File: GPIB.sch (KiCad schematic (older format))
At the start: 24 parts, among them P1 CONN_6, P2 CONN_2, P3 CONN_4X2, P4 CONN_CENTRONICS_24, SW1 SW_RESET, SW2 SW_BOOTL, U5 STM32F072CBT6, U6 SN75160B, U7 SN75162B

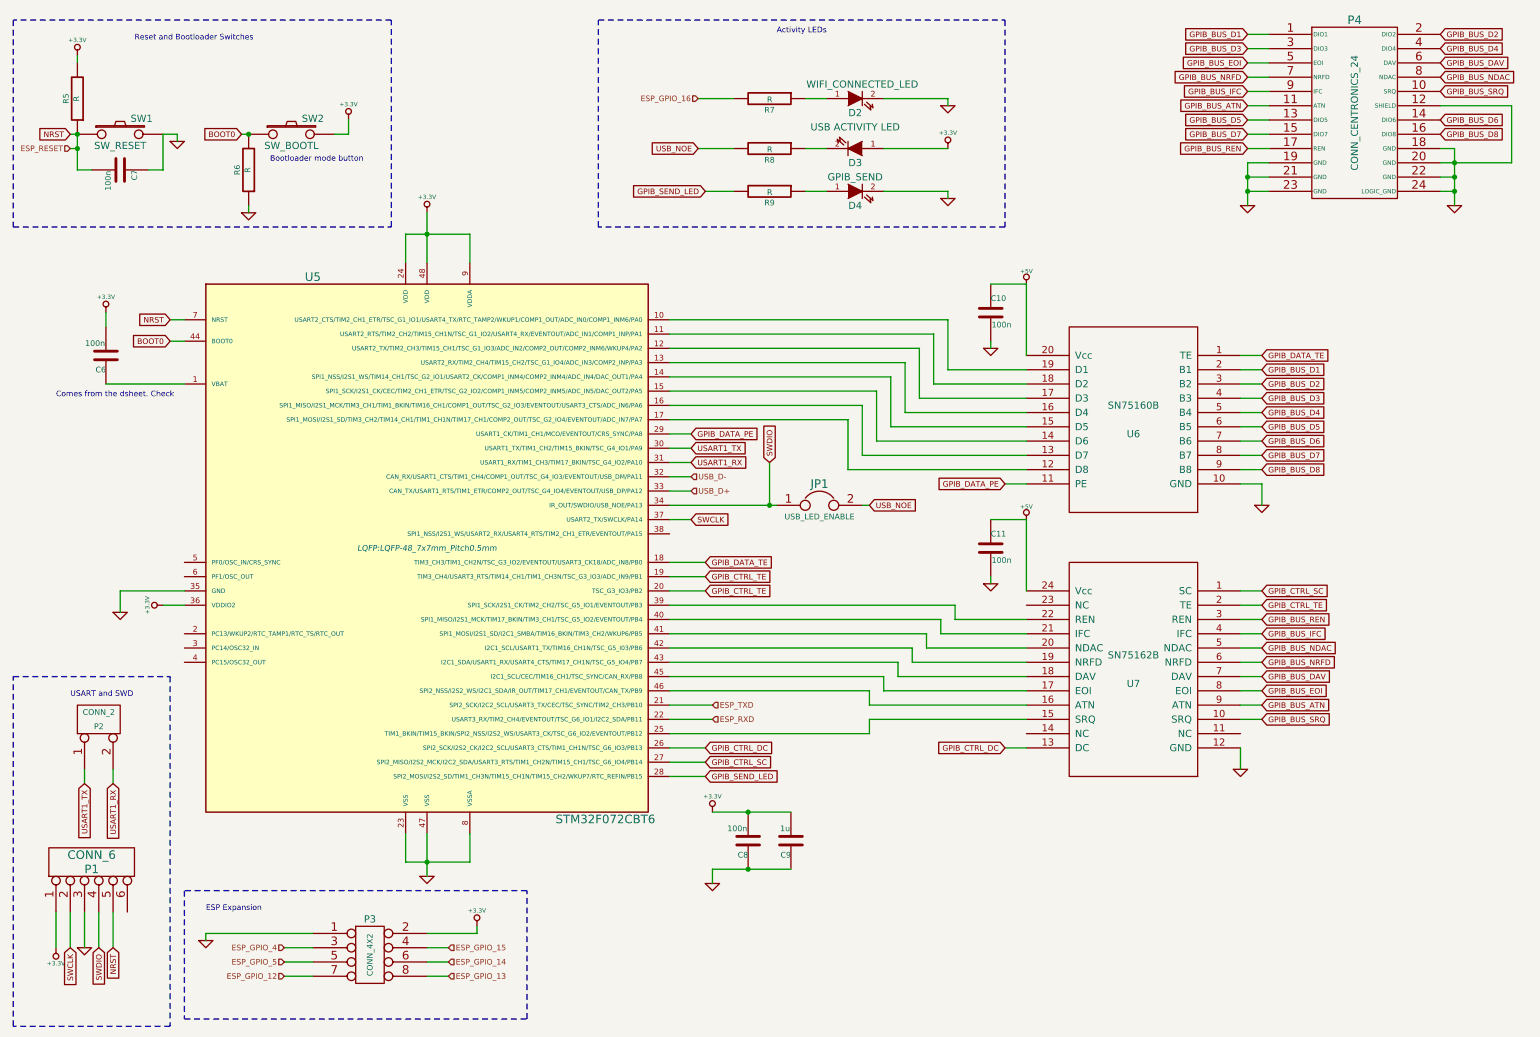
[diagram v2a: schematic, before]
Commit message: Remove Barrel Jack and associated power circuits. Unnecessary for now and add a lot of complexity / BOM cost
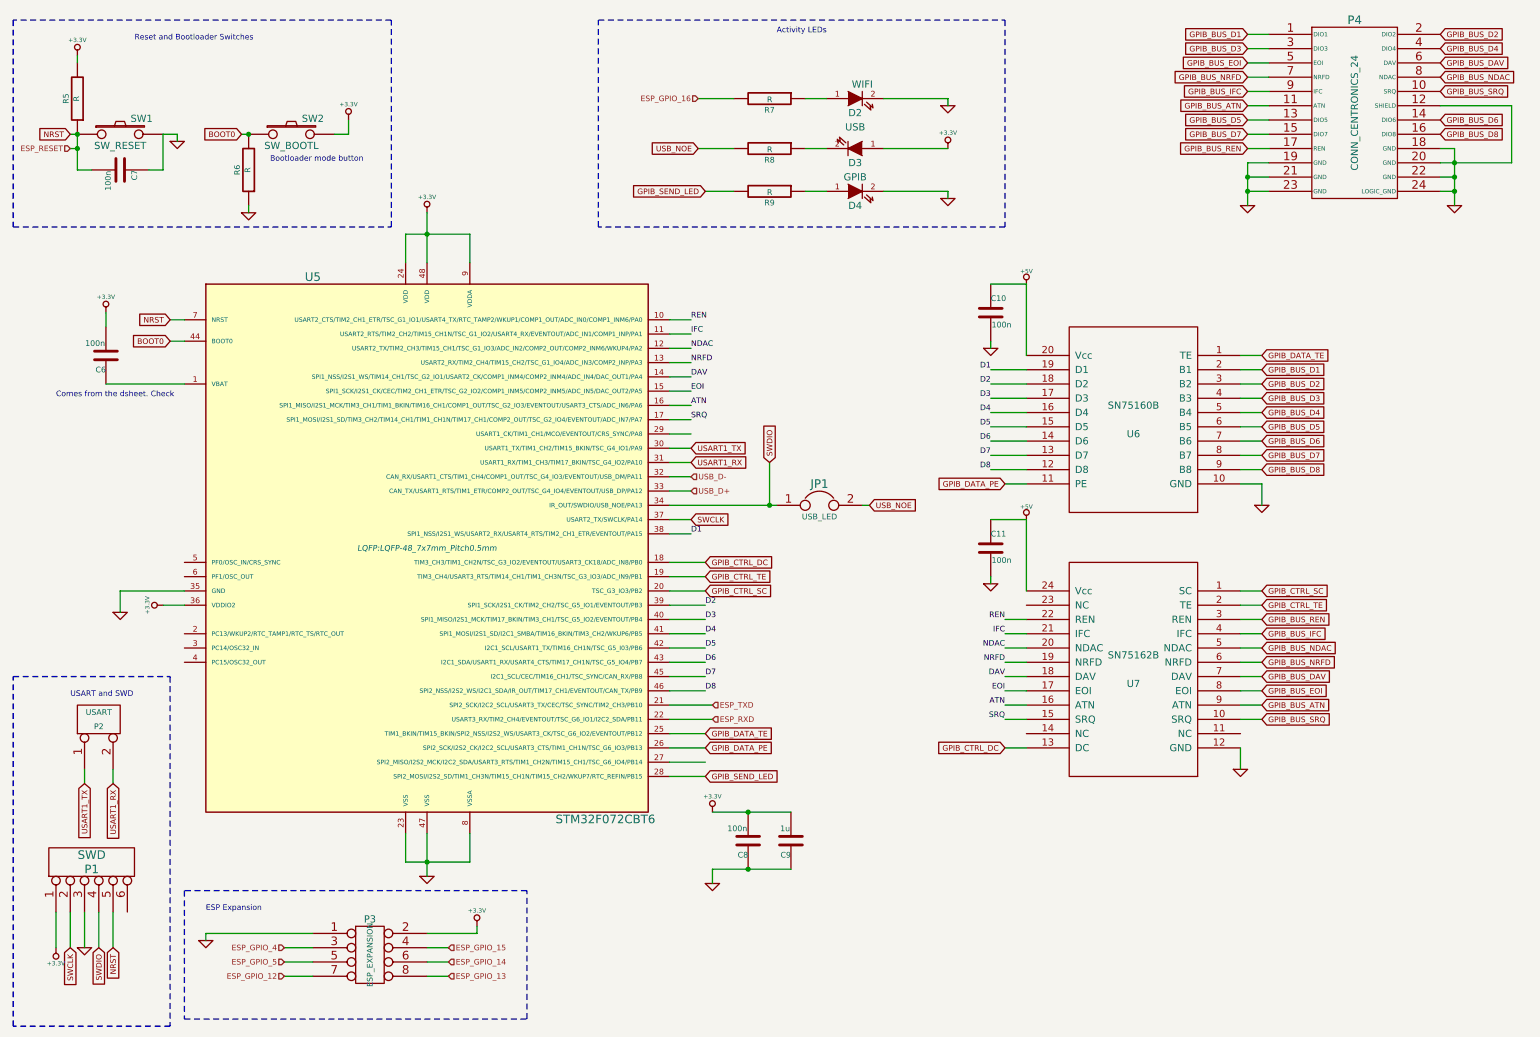
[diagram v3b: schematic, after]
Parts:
- D2: value WIFI_CONNECTED_LED -> WIFI
- D3: value USB ACTIVITY LED -> USB
- D4: value GPIB_SEND -> GPIB
- JP1: value USB_LED_ENABLE -> USB_LED
- P1: value CONN_6 -> SWD
- P2: value CONN_2 -> USART
- P3: value CONN_4X2 -> ESP_EXPANSION
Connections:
- net GPIB_CTRL_DC: now also U5.18 (TIM3_CH3/TIM1_CH2N/TSC_G3_IO2/EVENTOUT/USART3_CK18/ADC_IN8/PB0); no longer U5.26 (SPI2_SCK/I2S2_CK/I2C2_SCL/USART3_CTS/TIM1_CH1N/TSC_G6_IO3/PB13)
- net GPIB_CTRL_SC: now also U5.20 (TSC_G3_IO3/PB2); no longer U5.27 (SPI2_MISO/I2S2_MCK/I2C2_SDA/USART3_RTS/TIM1_CH2N/TIM15_CH1/TSC_G6_IO4/PB14)
- net GPIB_CTRL_TE: no longer U5.20 (TSC_G3_IO3/PB2)
- net GPIB_DATA_PE: now also U5.26 (SPI2_SCK/I2S2_CK/I2C2_SCL/USART3_CTS/TIM1_CH1N/TSC_G6_IO3/PB13); no longer U5.29 (USART1_CK/TIM1_CH1/MCO/EVENTOUT/CRS_SYNC/PA8)
- net GPIB_DATA_TE: now also U5.25 (TIM1_BKIN/TIM15_BKIN/SPI2_NSS/I2S2_WS/USART3_CK/TSC_G6_IO2/EVENTOUT/PB12); no longer U5.18 (TIM3_CH3/TIM1_CH2N/TSC_G3_IO2/EVENTOUT/USART3_CK18/ADC_IN8/PB0)
- net D8: now reaches U6.12 (D8)
- net D8: now also U5.46 (SPI2_NSS/I2S2_WS/I2C1_SDA/IR_OUT/TIM17_CH1/EVENTOUT/CAN_TX/PB9); no longer U5.17 (SPI1_MOSI/I2S1_SD/TIM3_CH2/TIM14_CH1/TIM1_CH1N/TIM17_CH1/COMP2_OUT/TSC_G2_IO4/EVENTOUT/ADC_IN7/PA7)
- net ATN: now reaches U5.16 (SPI1_MISO/I2S1_MCK/TIM3_CH1/TIM1_BKIN/TIM16_CH1/COMP1_OUT/TSC_G2_IO3/EVENTOUT/USART3_CTS/ADC_IN6/PA6)
- net ATN: now also U7.16 (ATN); no longer U6.13 (D7)
- net D6: now reaches U6.14 (D6)
- net D6: now also U5.43 (I2C1_SDA/USART1_RX/USART4_CTS/TIM17_CH1N/TSC_G5_IO4/PB7); no longer U5.15 (SPI1_SCK/I2S1_CK/CEC/TIM2_CH1_ETR/TSC_G2_IO2/COMP1_INM5/COMP2_INM5/ADC_IN5/DAC_OUT2/PA5)
- net D5: now reaches U6.15 (D5)
- net D5: now also U5.42 (I2C1_SCL/USART1_TX/TIM16_CH1N/TSC_G5_I03/PB6); no longer U5.14 (SPI1_NSS/I2S1_WS/TIM14_CH1/TSC_G2_IO1/USART2_CK/COMP1_INM4/COMP2_INM4/ADC_IN4/DAC_OUT1/PA4)
- net D4: now reaches U6.16 (D4)
- net D4: now also U5.41 (SPI1_MOSI/I2S1_SD/I2C1_SMBA/TIM16_BKIN/TIM3_CH2/WKUP6/PB5); no longer U5.13 (USART2_RX/TIM2_CH4/TIM15_CH2/TSC_G1_IO4/ADC_IN3/COMP2_INP/PA3)
- net D3: now reaches U6.17 (D3)
- net D3: now also U5.40 (SPI1_MISO/I2S1_MCK/TIM17_BKIN/TIM3_CH1/TSC_G5_IO2/EVENTOUT/PB4); no longer U5.12 (USART2_TX/TIM2_CH3/TIM15_CH1/TSC_G1_IO3/ADC_IN2/COMP2_OUT/COMP2_INM6/WKUP4/PA2)
- net D2: now reaches U6.18 (D2)
- net D2: now also U5.39 (SPI1_SCK/I2S1_CK/TIM2_CH2/TSC_G5_IO1/EVENTOUT/PB3); no longer U5.11 (USART2_RTS/TIM2_CH2/TIM15_CH1N/TSC_G1_IO2/USART4_RX/EVENTOUT/ADC_IN1/COMP1_INP/PA1)
- net D1: now reaches U6.19 (D1)
- net D1: now also U5.38 (SPI1_NSS/I2S1_WS/USART2_RX/USART4_RTS/TIM2_CH1_ETR/EVENTOUT/PA15); no longer U5.10 (USART2_CTS/TIM2_CH1_ETR/TSC_G1_IO1/USART4_TX/RTC_TAMP2/WKUP1/COMP1_OUT/ADC_IN0/COMP1_INM6/PA0)
- net SRQ: now reaches U7.15 (SRQ)
- net SRQ: now also U5.17 (SPI1_MOSI/I2S1_SD/TIM3_CH2/TIM14_CH1/TIM1_CH1N/TIM17_CH1/COMP2_OUT/TSC_G2_IO4/EVENTOUT/ADC_IN7/PA7); no longer U5.25 (TIM1_BKIN/TIM15_BKIN/SPI2_NSS/I2S2_WS/USART3_CK/TSC_G6_IO2/EVENTOUT/PB12)
- net D7: now reaches U5.45 (I2C1_SCL/CEC/TIM16_CH1/TSC_SYNC/CAN_RX/PB8)
- net D7: now also U6.13 (D7); no longer U7.17 (EOI)
- net DAV: now reaches U7.18 (DAV)
- net DAV: now also U5.14 (SPI1_NSS/I2S1_WS/TIM14_CH1/TSC_G2_IO1/USART2_CK/COMP1_INM4/COMP2_INM4/ADC_IN4/DAC_OUT1/PA4); no longer U5.43 (I2C1_SDA/USART1_RX/USART4_CTS/TIM17_CH1N/TSC_G5_IO4/PB7)
- net NRFD: now reaches U7.19 (NRFD)
- net NRFD: now also U5.13 (USART2_RX/TIM2_CH4/TIM15_CH2/TSC_G1_IO4/ADC_IN3/COMP2_INP/PA3); no longer U5.42 (I2C1_SCL/USART1_TX/TIM16_CH1N/TSC_G5_I03/PB6)
- net NDAC: now reaches U7.20 (NDAC)
- net NDAC: now also U5.12 (USART2_TX/TIM2_CH3/TIM15_CH1/TSC_G1_IO3/ADC_IN2/COMP2_OUT/COMP2_INM6/WKUP4/PA2); no longer U5.41 (SPI1_MOSI/I2S1_SD/I2C1_SMBA/TIM16_BKIN/TIM3_CH2/WKUP6/PB5)
- net IFC: now reaches U7.21 (IFC)
- net IFC: now also U5.11 (USART2_RTS/TIM2_CH2/TIM15_CH1N/TSC_G1_IO2/USART4_RX/EVENTOUT/ADC_IN1/COMP1_INP/PA1); no longer U5.40 (SPI1_MISO/I2S1_MCK/TIM17_BKIN/TIM3_CH1/TSC_G5_IO2/EVENTOUT/PB4)
- net REN: now reaches U7.22 (REN)
- net REN: now also U5.10 (USART2_CTS/TIM2_CH1_ETR/TSC_G1_IO1/USART4_TX/RTC_TAMP2/WKUP1/COMP1_OUT/ADC_IN0/COMP1_INM6/PA0); no longer U5.39 (SPI1_SCK/I2S1_CK/TIM2_CH2/TSC_G5_IO1/EVENTOUT/PB3)
- new net EOI: U5.15 (SPI1_SCK/I2S1_CK/CEC/TIM2_CH1_ETR/TSC_G2_IO2/COMP1_INM5/COMP2_INM5/ADC_IN5/DAC_OUT2/PA5), U7.17 (EOI)
